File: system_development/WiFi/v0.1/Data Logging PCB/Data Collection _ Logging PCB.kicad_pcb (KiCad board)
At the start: 2 copper layers, 34.3 x 53.3 mm, 8 parts, among them U1 TC2014-3.3VxCTTR

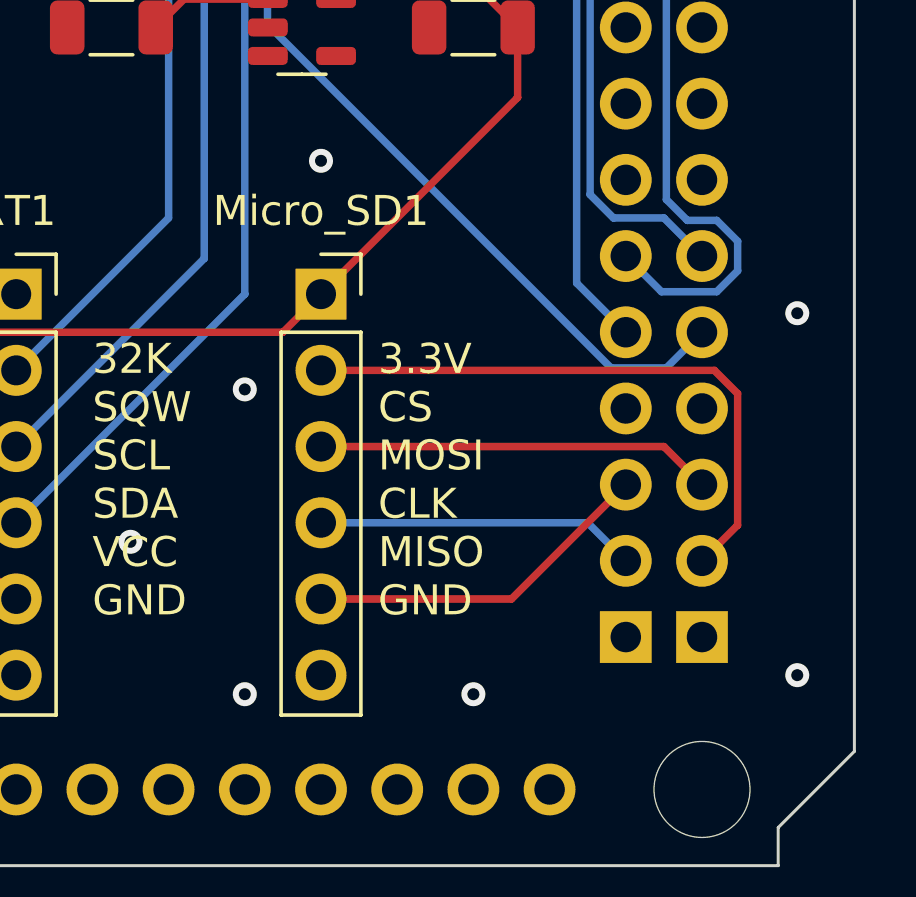
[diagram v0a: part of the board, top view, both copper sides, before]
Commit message: Redid PCB's for Wifi Version
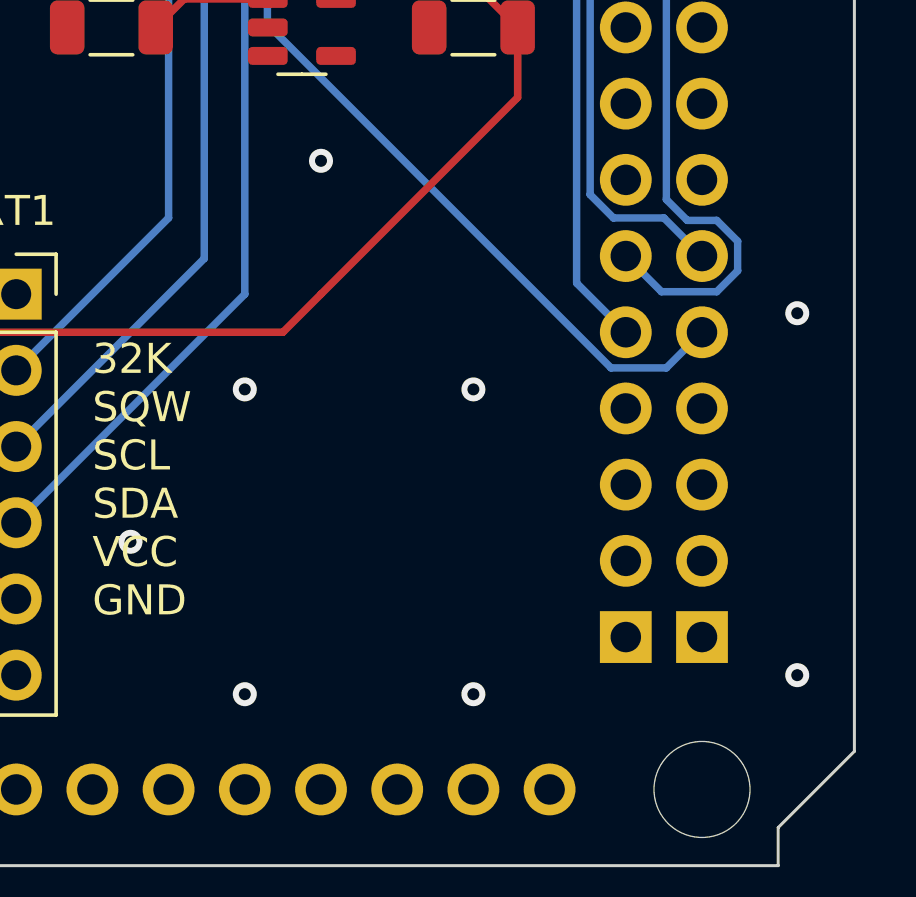
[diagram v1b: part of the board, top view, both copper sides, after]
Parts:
- removed Micro_SD1: microSD_small, Connector_PinSocket_2.54mm:PinSocket_1x06_P2.54mm_Vertical
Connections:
- XA1 pad D50: Net-(Micro_SD1-MISO) -> unconnected-(XA1-PadD50)
- XA1 pad D51: Net-(Micro_SD1-MOSI) -> unconnected-(XA1-PadD51)
- XA1 pad D52: Net-(Micro_SD1-CLK) -> unconnected-(XA1-PadD52)
- XA1 pad D53: Net-(Micro_SD1-CS) -> unconnected-(XA1-D53_SS-PadD53)
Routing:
- net Net-(Micro_SD1-CS): track 20.3 -> 0.00 mm
- net Net-(Micro_SD1-MOSI): track 13.2 -> 0.00 mm
- net Net-(Micro_SD1-MISO): track 11.7 -> 0.00 mm
- net Net-(Micro_SD1-CLK): track 10.7 -> 0.00 mm
- net GND: vias 10 -> 11
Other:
- board text added: "Wifi-Datalogging v0.1 6/21/2024 Nicholas Liger ARTS Lab - USC"
- board text removed: "3.3V CS MOSI CLK MISO GND"
- board text removed: "Datalogging v0.2 5/16/2024 Nicholas Liger ARTS Lab - USC"
